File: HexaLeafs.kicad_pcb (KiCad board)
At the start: 2 copper layers, 104 x 90 mm, 25 parts, among them J1 Conn_01x04, J2 Conn_01x04, J3 Conn_01x04, J4 Conn_01x04, J5 Conn_01x04, J6 Conn_01x04

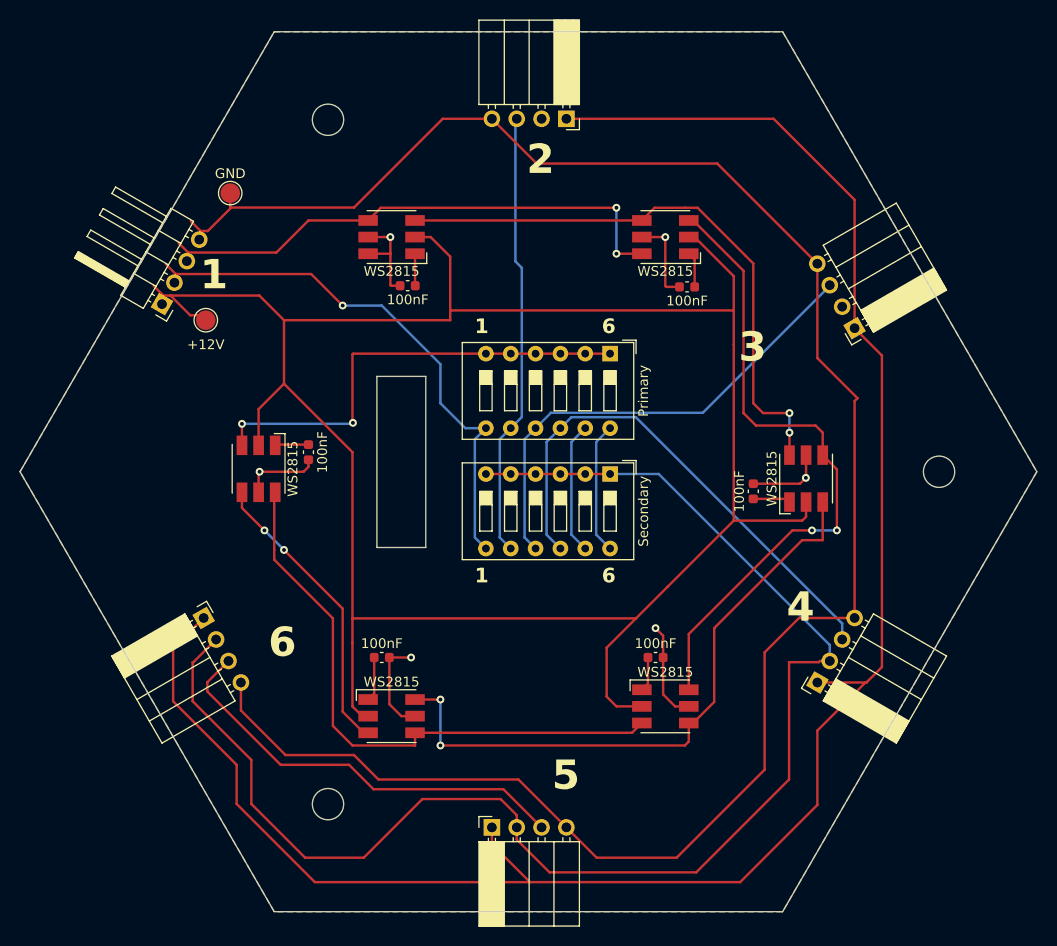
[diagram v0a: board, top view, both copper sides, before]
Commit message: Align Traces and Connectors
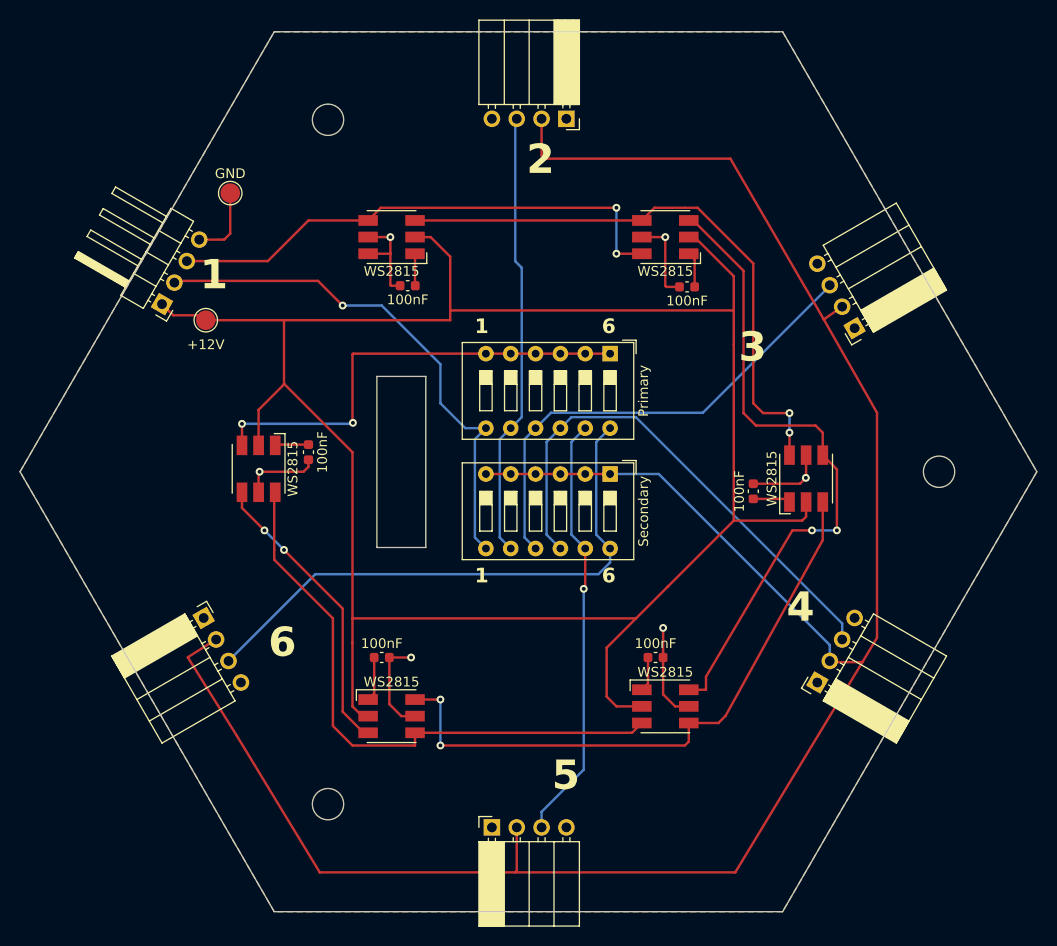
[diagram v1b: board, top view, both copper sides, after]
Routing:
- net +12V: track 425.0 -> 218.6 mm
- net GND: track 259.3 -> 62.5 mm
- net 2nd In: track 149.2 -> 230.4 mm
- net Out6: track 13.8 -> 58.4 mm
- net Out2: track 89.6 -> 45.7 mm
- net Out5: track 13.5 -> 43.9 mm, vias 0 -> 1
- net Out1: track 55.3 -> 53.8 mm
- net Net-(U3-DO): track 64.5 -> 63.3 mm
- net WS_Input: track 54.4 -> 53.5 mm
- net Net-(U2-DO): track 67.4 -> 66.8 mm
